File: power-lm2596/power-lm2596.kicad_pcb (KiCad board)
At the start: 2 copper layers, 34.3 x 72.4 mm, 10 parts, among them J1 Screw_Terminal_01x04, J3 Conn_01x06_Female, SW1 SW_DIP_x02, U1 LM2596-Board

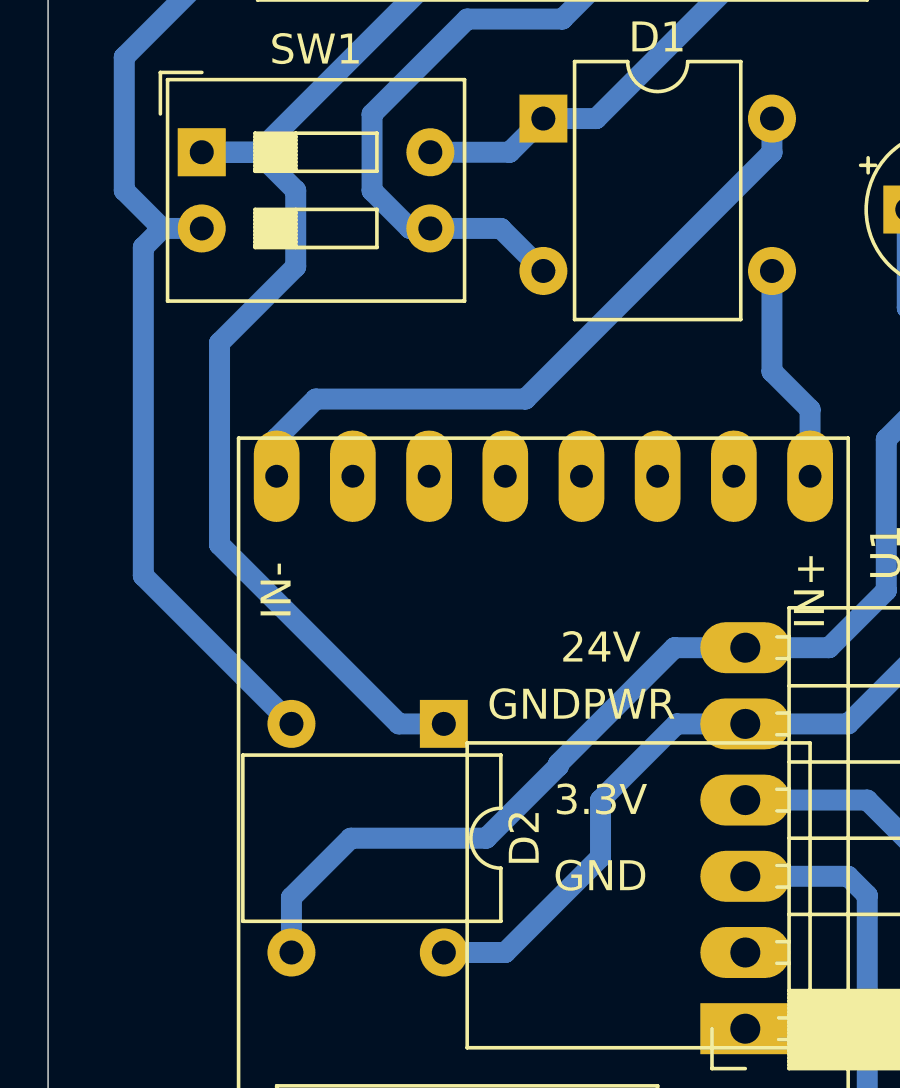
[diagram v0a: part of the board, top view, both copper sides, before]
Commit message: update power-lm2596 routing
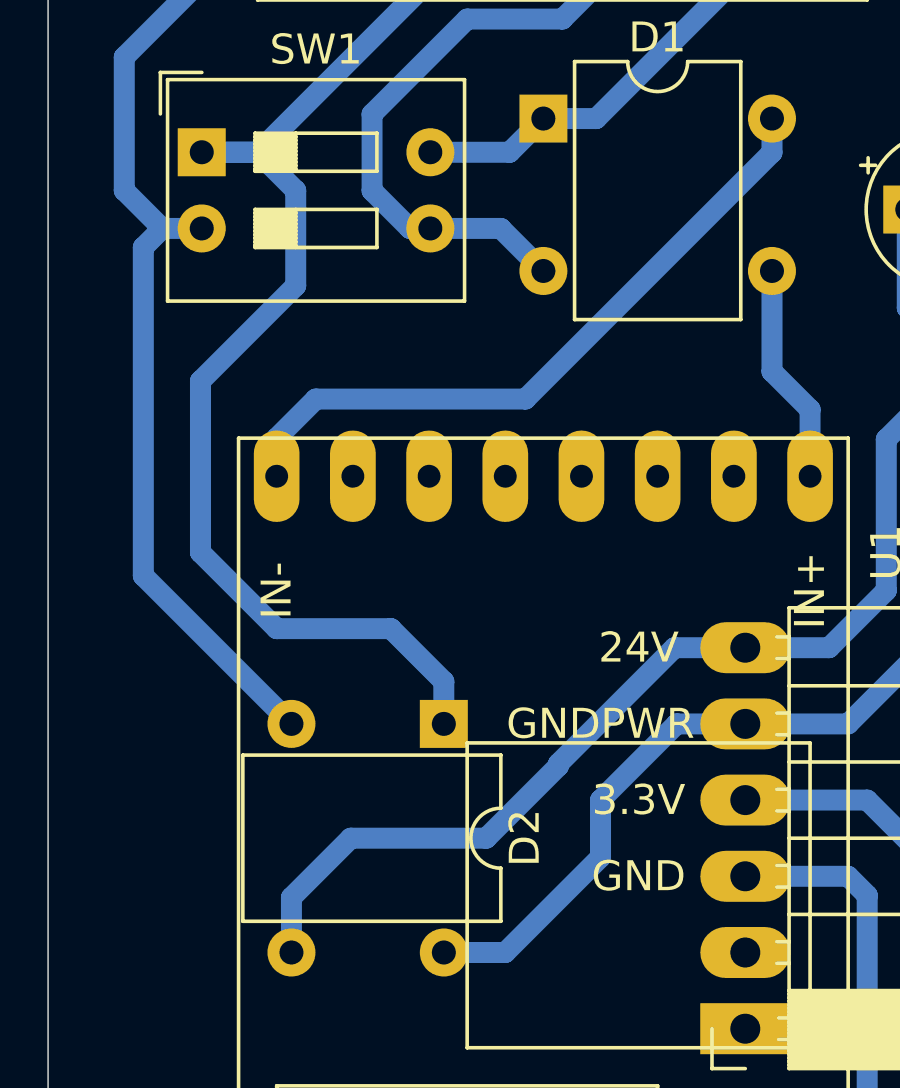
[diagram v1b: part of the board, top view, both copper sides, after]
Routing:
- net FIELD-: track 40.4 -> 42.3 mm
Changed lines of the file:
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@@
     (pad "" thru_hole oval locked (at 20.447 -6.35 270) (size 3.048 1.524) (drill 0.762) (layers *.Cu *.Mask))
     (pad "1" thru_hole oval locked (at -20.32 -8.89 270) (size 3.048 1.524) (drill 0.762) (layers *.Cu *.Mask)
-      (net 7 "Net-(D1-Pad3)") (pinfunction "IN+") (pintype "power_in"))
+      (net 7 "Net-(D1-Pad3)") (pinfunction "IN+"))
     (pad "2" thru_hole oval locked (at -20.32 8.89 270) (size 3.048 1.524) (drill 0.762) (layers *.Cu *.Mask)
-      (net 5 "Net-(D1-Pad4)") (pinfunction "IN-") (pintype "power_in"))
+      (net 5 "Net-(D1-Pad4)") (pinfunction "IN-"))
     (pad "3" thru_hole oval locked (at 20.447 8.89 270) (size 3.048 1.524) (drill 0.762) (layers *.Cu *.Mask)
-      (net 4 "GND") (pinfunction "OUT-") (pintype "power_out"))
+      (net 4 "GND") (pinfunction "OUT-"))
     (pad "4" thru_hole oval locked (at 20.447 -8.89 270) (size 3.048 1.524) (drill 0.762) (layers *.Cu *.Mask)
-      (net 3 "+3V3") (pinfunction "OUT+") (pintype "power_out"))
+      (net 3 "+3V3") (pinfunction "OUT+"))
     (model "${KISYS3DMOD}/Connector_PinSocket_2.54mm.3dshapes/PinSocket_1x08_P2.54mm_Vertical.step"
       (offset (xyz 20.447 8.89 0))
@@
   (gr_arc (start 95.25 124.46) (end 95.25 127) (angle -90) (layer "Edge.Cuts") (width 0.05))
   (gr_arc (start 95.25 57.15) (end 97.79 57.15) (angle -90) (layer "Edge.Cuts") (width 0.05))
-  (gr_text "24V" (at 81.915 86.36) (layer "F.SilkS")
+  (gr_text "24V" (at 83.185 86.36) (layer "F.SilkS")
     (effects (font (size 1 1) (thickness 0.15)))
   )
-  (gr_text "GND" (at 81.915 93.98) (layer "F.SilkS")
+  (gr_text "GND" (at 83.185 93.98) (layer "F.SilkS")
     (effects (font (size 1 1) (thickness 0.15)))
   )
-  (gr_text "3.3V" (at 81.915 91.44) (layer "F.SilkS")
+  (gr_text "3.3V" (at 83.185 91.44) (layer "F.SilkS")
     (effects (font (size 1 1) (thickness 0.15)))
   )
-  (gr_text "GNDPWR" (at 81.28 88.265) (layer "F.SilkS")
+  (gr_text "GNDPWR" (at 81.915 88.9) (layer "F.SilkS")
     (effects (font (size 1 1) (thickness 0.15)))
   )
@@
     (pts (xy 97.79 52.07) (xy 63.5 52.07))
     (height 0)
-    (gr_text "34,2900 mm" (at 80.645 50.92) (layer "Dwgs.User")
+    (gr_text "34.2900 mm" (at 80.645 50.92) (layer "Dwgs.User")
       (effects (font (size 1 1) (thickness 0.15)))
     )
@@
     (pts (xy 102.87 90.17) (xy 102.87 54.61))
     (height 0)
-    (gr_text "1,4000 in" (at 101.72 72.39 90) (layer "Dwgs.User")
+    (gr_text "1.4000 in" (at 101.72 72.39 90) (layer "Dwgs.User")
       (effects (font (size 1 1) (thickness 0.15)))
     )
@@
     (pts (xy 101.6 99.06) (xy 101.6 127))
     (height -1.27)
-    (gr_text "1,1000 in" (at 101.72 113.03 90) (layer "Dwgs.User")
+    (gr_text "1.1000 in" (at 101.72 113.03 90) (layer "Dwgs.User")
       (effects (font (size 1 1) (thickness 0.15)))
     )
@@
   (segment (start 66.675 83.9625) (end 66.675 73.015) (width 0.7) (layer "B.Cu") (net 9))
   (segment (start 66.675 73.015) (end 67.305 72.385) (width 0.7) (layer "B.Cu") (net 9))
-  (segment (start 71.755 71.12) (end 70.48 69.845) (width 0.7) (layer "B.Cu") (net 10))
+  (segment (start 76.6925 88.9) (end 76.6925 87.4875) (width 0.7) (layer "B.Cu") (net 10))
+  (segment (start 71.755 74.295) (end 71.755 71.12) (width 0.7) (layer "B.Cu") (net 10))
+  (segment (start 71.12 85.725) (end 68.58 83.185) (width 0.7) (layer "B.Cu") (net 10))
+  (segment (start 68.58 77.47) (end 71.755 74.295) (width 0.7) (layer "B.Cu") (net 10))
+  (segment (start 76.6925 87.4875) (end 74.93 85.725) (width 0.7) (layer "B.Cu") (net 10))
+  (segment (start 78.105 62.23) (end 70.49 69.845) (width 0.7) (layer "B.Cu") (net 10))
   (segment (start 70.48 69.845) (end 68.6225 69.845) (width 0.7) (layer "B.Cu") (net 10))
-  (segment (start 69.215 82.9225) (end 69.215 76.2) (width 0.7) (layer "B.Cu") (net 10))
-  (segment (start 76.6925 88.9) (end 75.1925 88.9) (width 0.7) (layer "B.Cu") (net 10))
-  (segment (start 78.105 62.23) (end 70.49 69.845) (width 0.7) (layer "B.Cu") (net 10))
-  (segment (start 75.1925 88.9) (end 69.215 82.9225) (width 0.7) (layer "B.Cu") (net 10))
   (segment (start 70.49 69.845) (end 68.6225 69.845) (width 0.7) (layer "B.Cu") (net 10))
   (segment (start 78.105 60.96) (end 78.105 62.23) (width 0.7) (layer "B.Cu") (net 10))
-  (segment (start 71.755 73.66) (end 71.755 71.12) (width 0.7) (layer "B.Cu") (net 10))
-  (segment (start 69.215 76.2) (end 71.755 73.66) (width 0.7) (layer "B.Cu") (net 10))
+  (segment (start 71.755 71.12) (end 70.48 69.845) (width 0.7) (layer "B.Cu") (net 10))
+  (segment (start 74.93 85.725) (end 71.12 85.725) (width 0.7) (layer "B.Cu") (net 10))
+  (segment (start 68.58 83.185) (end 68.58 77.47) (width 0.7) (layer "B.Cu") (net 10))
 )

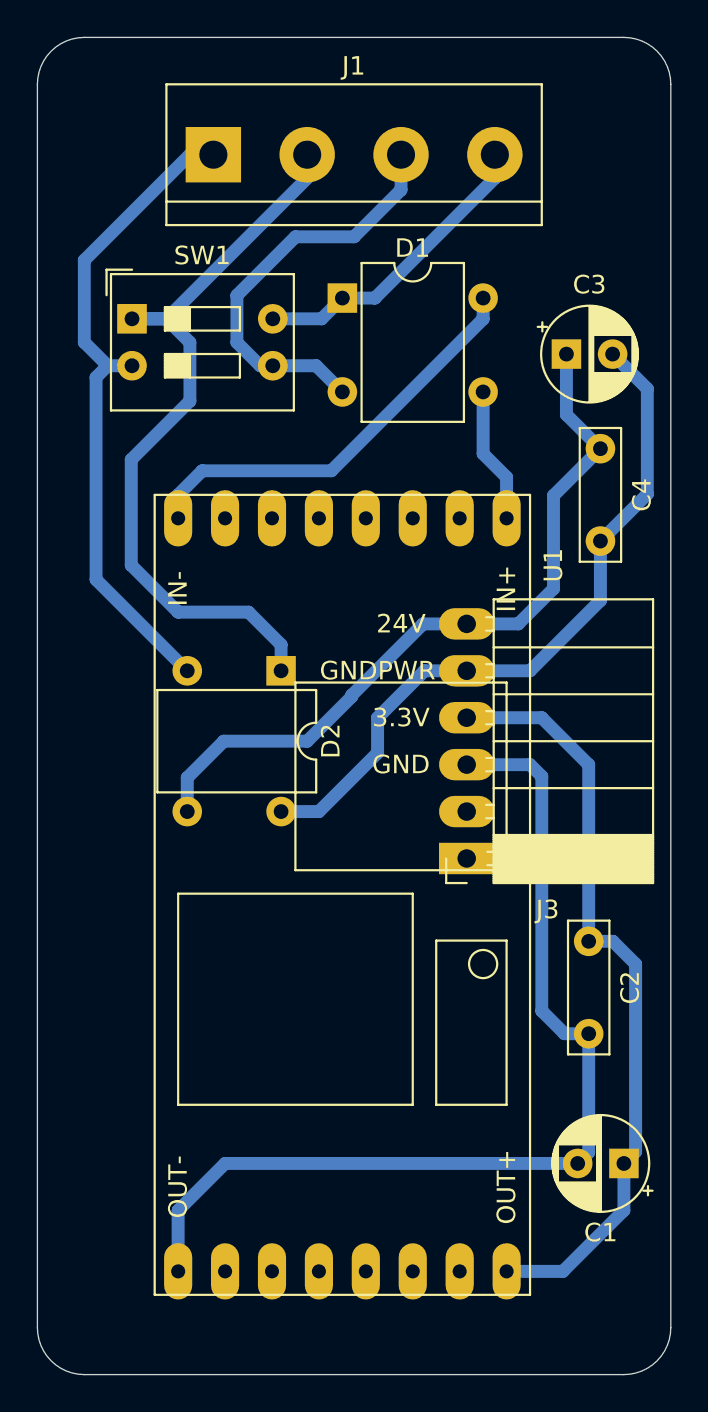
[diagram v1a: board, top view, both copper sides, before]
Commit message: refactor power-lm2596
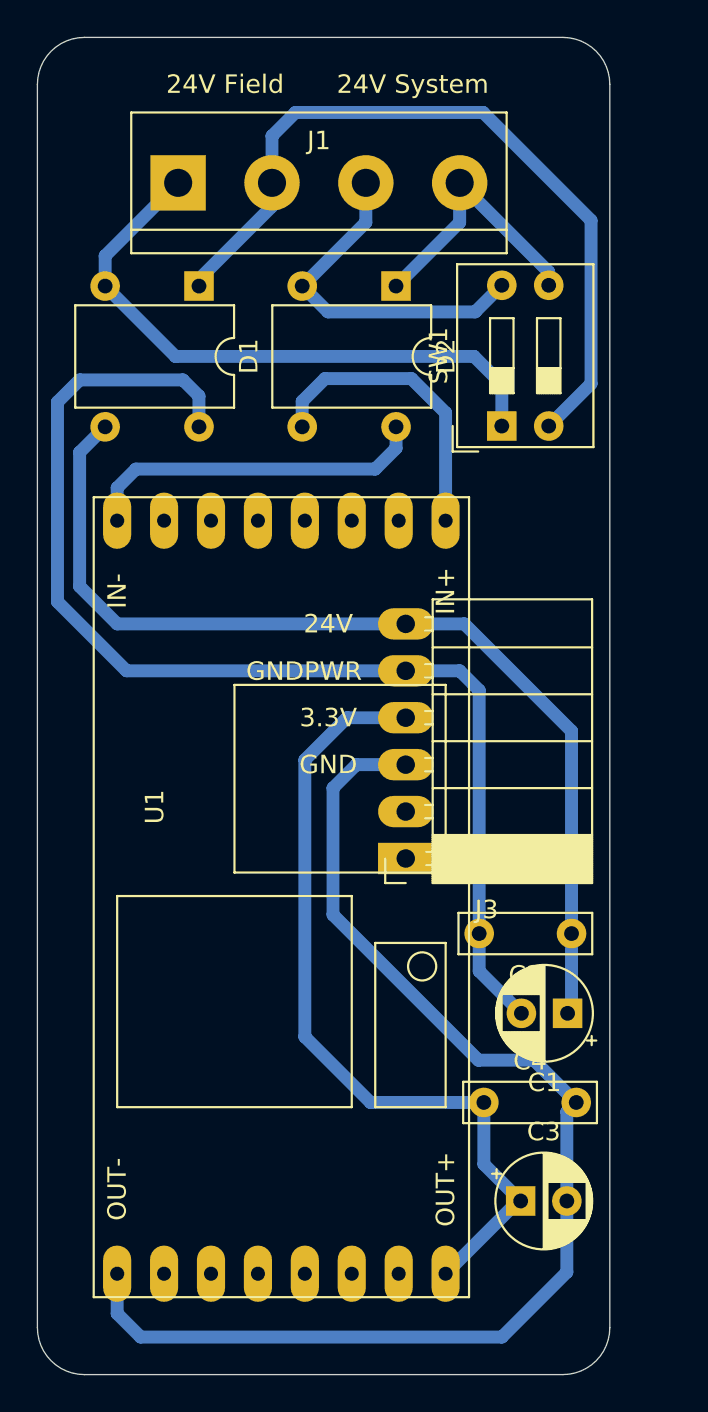
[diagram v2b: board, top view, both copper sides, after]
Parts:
- C2: value 100nF 63V -> 100nF 50V
- C4: value 100nF 50V -> 100nF 63V
- moved C3 45.9 mm to (89.7, 117.6)
- moved C4 36.0 mm to (87.7, 112.3), turned to 0 degrees
- moved D2 21.7 mm to (82.9, 68.1)
- moved SW1 20.8 mm to (88.6, 75.6), turned to 90 degrees
- moved C1 8.68 mm to (92.2, 107.4)
- moved D1 7.79 mm to (72.2, 68.1), turned to -90 degrees
- moved U1 3.30 mm to (76.7, 101.1)
- moved J3 3.30 mm to (83.4, 99.1)
- moved J1 2.44 mm to (71.1, 62.5)
- moved C2 1.02 mm to (92.4, 103.1), turned to 180 degrees
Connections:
- C1 pad 1: +3V3 -> +24V
- C1 pad 2: GND -> GNDPWR
- C2 pad 1: +3V3 -> +24V
- C2 pad 2: GND -> GNDPWR
- C3 pad 1: +24V -> +3V3
- C3 pad 2: GNDPWR -> GND
- C4 pad 1: +24V -> +3V3
- C4 pad 2: GNDPWR -> GND
- D1 pad 1: SYSTEM- -> FIELD-
- D1 pad 2: SYSTEM+ -> FIELD+
- D1 pad 3: Net-(D1-Pad3) -> +24V
- D1 pad 4: Net-(D1-Pad4) -> GNDPWR
- D2 pad 1: FIELD- -> SYSTEM-
- D2 pad 2: FIELD+ -> SYSTEM+
- D2 pad 3: +24V -> Net-(D2-Pad3)
- D2 pad 4: GNDPWR -> Net-(D2-Pad4)
- SW1 pad 1: FIELD- -> FIELD+
- SW1 pad 2: FIELD+ -> FIELD-
- SW1 pad 3: SYSTEM+ -> SYSTEM-
- SW1 pad 4: SYSTEM- -> SYSTEM+
- U1 pad 1: Net-(D1-Pad3) -> Net-(D2-Pad3)
- U1 pad 2: Net-(D1-Pad4) -> Net-(D2-Pad4)
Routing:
- net GNDPWR: track 38.3 -> 64.2 mm
- net Net-(D1-Pad4): track 22.9 -> 0.00 mm
- net Net-(D2-Pad4): track 0.00 -> 18.9 mm
- net Net-(D2-Pad3): track 0.00 -> 16.3 mm
- net +24V: track 40.5 -> 54.5 mm
- net GND: track 53.3 -> 66.6 mm
- net Net-(D1-Pad3): track 7.37 -> 0.00 mm
- net SYSTEM+: track 22.5 -> 19.0 mm
- net +3V3: track 41.6 -> 44.4 mm
- net FIELD+: track 35.7 -> 33.2 mm
- net SYSTEM-: track 16.4 -> 14.6 mm
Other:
- board size 34.3 x 72.4 mm -> 31 x 72.4 mm
- board text added: "24V Field"
- board text added: "24V System"
